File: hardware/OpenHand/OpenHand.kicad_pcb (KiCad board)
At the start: 4 copper layers, 110 x 50 mm, 214 parts, among them J1 CONN_MOTOR_1, J10 CONN_JTAG, J11 CONN_FDBK_2, J12 CONN_EMG_2, J13 CONN_POS_3, J2 CONN_MOTOR_2, J3 CONN_BATT, J4 CONN_POS_1, J5 USB_C_CONN, J6 CONN_MOTOR_3, J7 CONN_FDBK_1, J8 CONN_EMG_1, J9 CONN_POS_2, Q1 AO3401A, SW1 BTN_RST, SW2 BTN_BOOT, SW3 SW_Push, U1 STM32F103RETx, U10 DRV8833PWP, U2 TPS565201DDCR, U3 AMS1117-3.3, U4 LT1175-5_SOT223, U5 LM324, U6 LM324, U7 DRV8833PWP, U8 DRV8833PWP, U9 DRV8833PWP

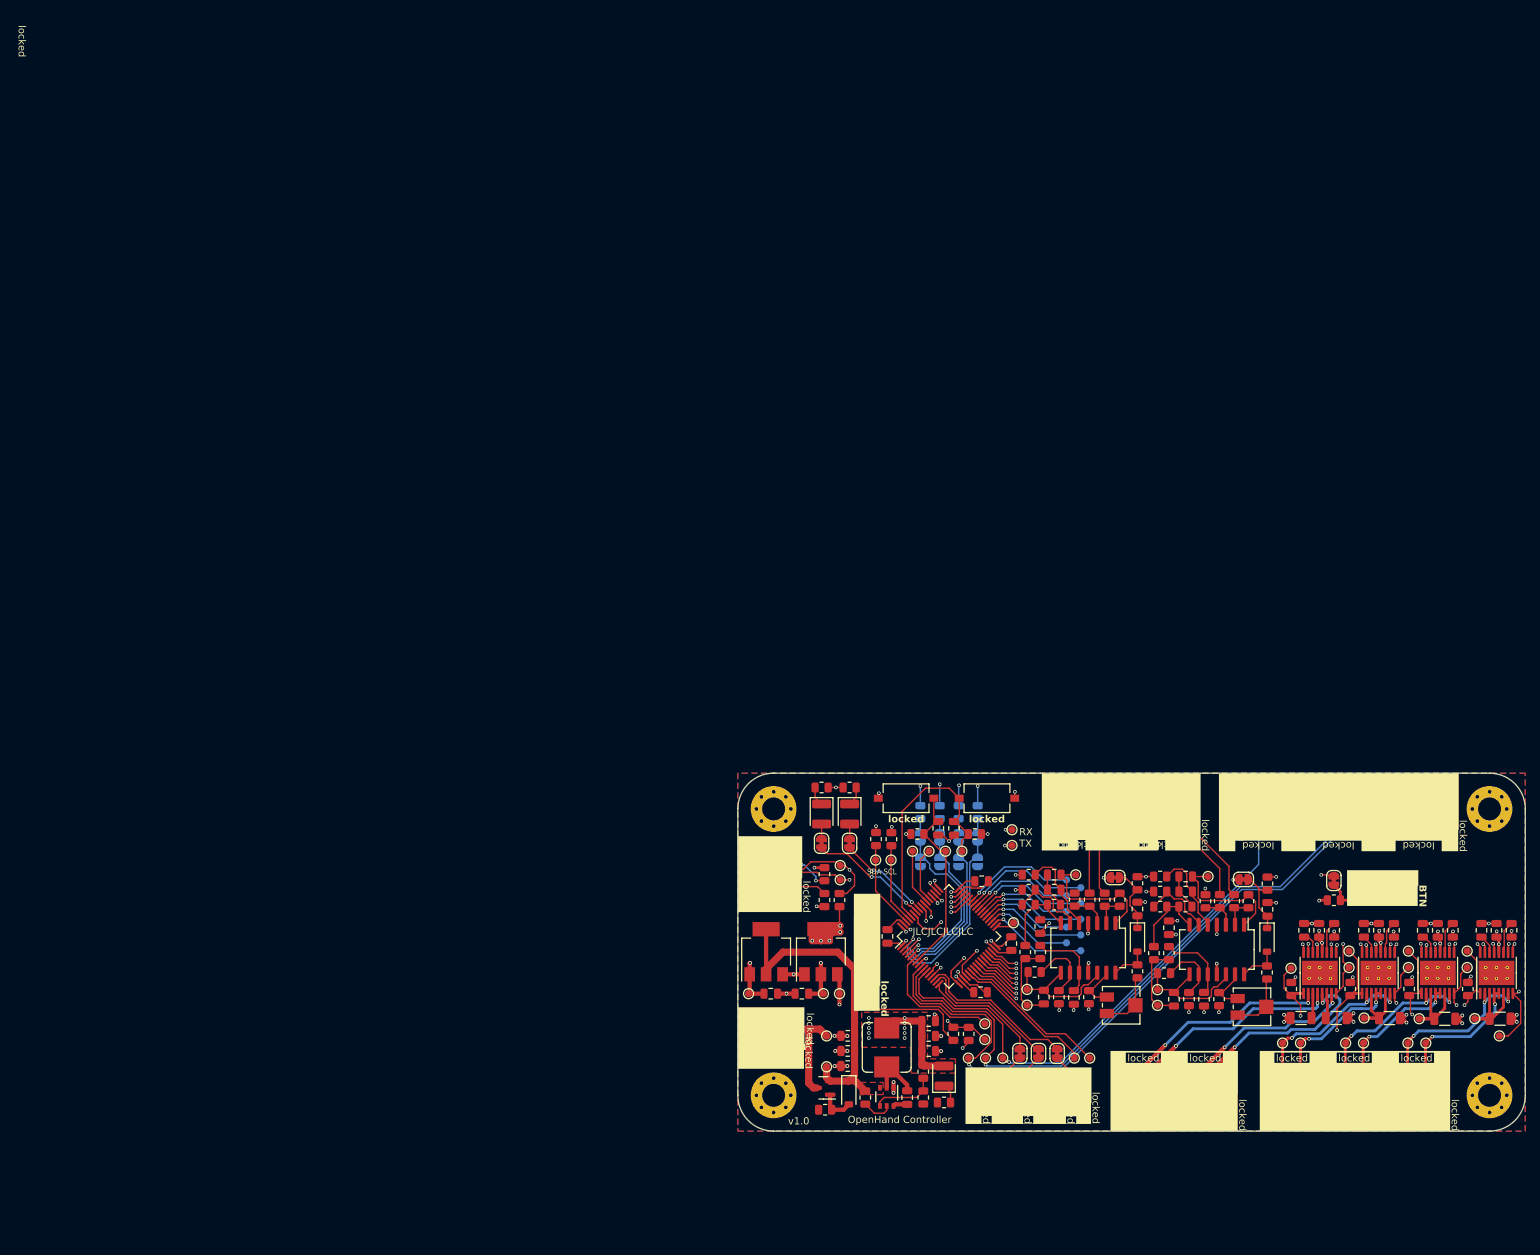
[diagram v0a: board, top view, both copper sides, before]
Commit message: Update PCB design/layout
Still WIP, routing traces currently
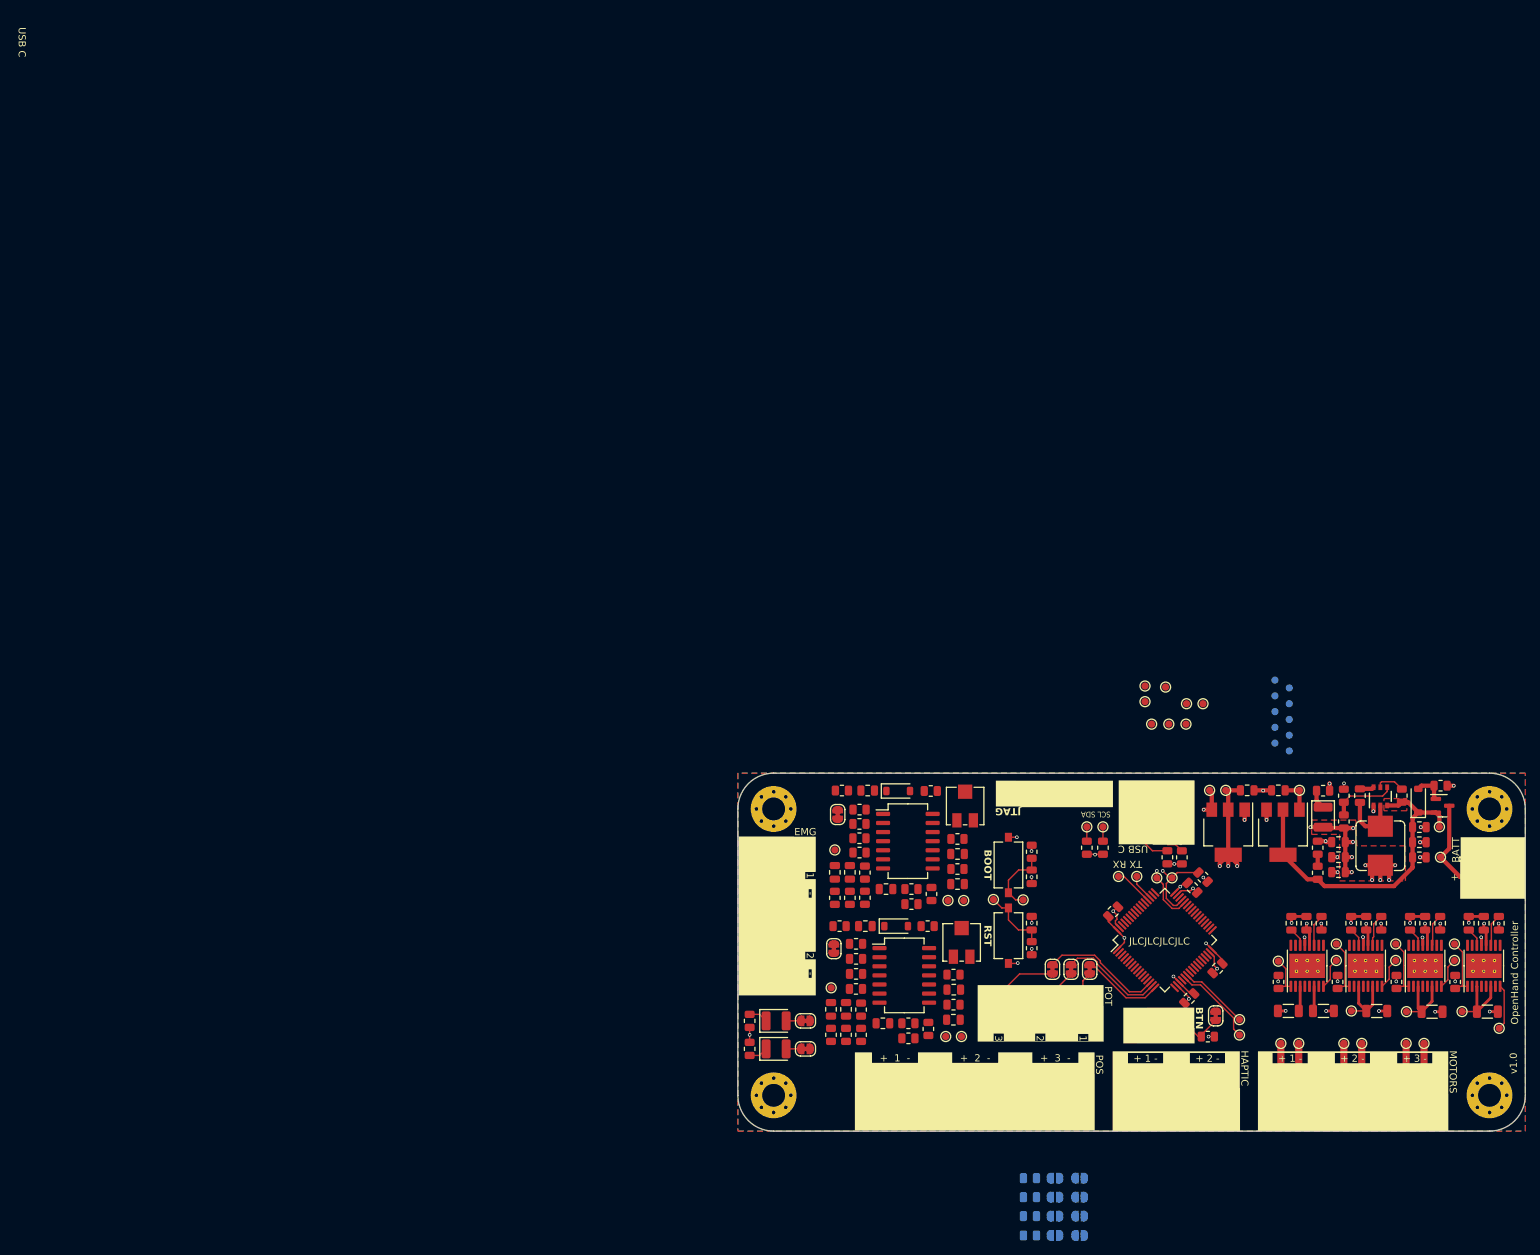
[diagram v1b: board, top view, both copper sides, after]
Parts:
- moved J3 99.3 mm to (203.0, 112.0), turned to -90 degrees
- moved R19 97.2 mm to (198.2, 101.8), turned to 180 degrees
- moved Q1 95.0 mm to (198.4, 104.5), turned to 0 degrees
- moved TP20 91.9 mm to (198.0, 107.5), turned to 180 degrees
- moved D3 89.4 mm to (195.1, 103.8), turned to 90 degrees
- moved TP19 89.3 mm to (198.2, 111.8), turned to 180 degrees
- moved C9 86.5 mm to (195.2, 107.5), turned to 0 degrees
- moved R17 86.0 mm to (192.8, 103.1), turned to -90 degrees
- moved C7 85.0 mm to (195.2, 109.6), turned to 0 degrees
- moved C8 83.7 mm to (195.2, 111.8), turned to 0 degrees
- moved TP23 82.0 mm to (178.4, 102.4), turned to 180 degrees
- moved U2 80.7 mm to (189.8, 103.2), turned to 90 degrees
- moved J4 76.9 mm to (124.4, 142.7), turned to 180 degrees
- moved C15 76.4 mm to (175.5, 102.4), turned to 180 degrees
- moved C10 76.0 mm to (186.9, 103.1), turned to 90 degrees
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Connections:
- net Net-(C18-Pad1) renamed /Sensors/amp_out_1
- J10 pad 3: JTAG_TDI -> JTAG_TDO
- J10 pad 4: JTAG_TDO -> JTAG_TDI
- U1 pad 14: TRIM_POT_01 -> TRIM_POT_03
- U1 pad 16: TRIM_POT_03 -> TRIM_POT_01
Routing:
- net MOTOR_03_DIR: track 120.6 -> 0.00 mm, vias 3 -> 0
- net MOTOR_03_PWM: track 112.1 -> 0.00 mm, vias 3 -> 0
- net MOTOR_02_DIR: track 111.6 -> 0.00 mm, vias 3 -> 0
- net HALL_SENS_01_S: track 102.2 -> 0.00 mm, vias 1 -> 0
- net MOTOR_02_PWM: track 102.1 -> 0.00 mm, vias 3 -> 0
- net HALL_SENS_02_S: track 86.8 -> 0.00 mm, vias 1 -> 0
- net MOTOR_01_DIR: track 84.6 -> 0.00 mm, vias 3 -> 0
- net MOTOR_01_PWM: track 82.9 -> 0.00 mm, vias 3 -> 0
- net MOTOR_03_FAULT: track 89.3 -> 6.39 mm, vias 2 -> 0
- net MOTOR_03_EN: track 87.5 -> 8.25 mm, vias 2 -> 0
- net -5V: track 80.5 -> 4.70 mm, vias 3 -> 0
- net HALL_SENS_03_S: track 74.8 -> 0.00 mm, vias 1 -> 0
- net MOTOR_02_EN: track 79.8 -> 8.23 mm, vias 2 -> 0
- net MOTOR_02_FAULT: track 75.5 -> 4.37 mm, vias 2 -> 0
- net BTN_01: track 68.1 -> 0.00 mm, vias 2 -> 0
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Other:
- board text added: "+"
- board text added: "+ 1 -"
- board text added: "+ 2 -"
- board text added: "+ 3 -"
- board text added: "-"
- board text added: "BATT"
- board text added: "BOOT"
- board text added: "EMG"
- board text added: "GND RST TDO TDI TCK TMS"
- board text added: "HAPTIC"
- board text added: "JTAG"
- board text added: "MOTORS"
- board text added: "POS"
- board text added: "POT"
- board text added: "RST"
- board text added: "SCL SDA"
- board text added: "TX RX"
- board text added: "USB C"
- board text added: "github.com/AleksaHeler/ProstheticHand"
- board text removed: "RX TX"
- board text removed: "SDA SCL"
- board text removed: "locked"

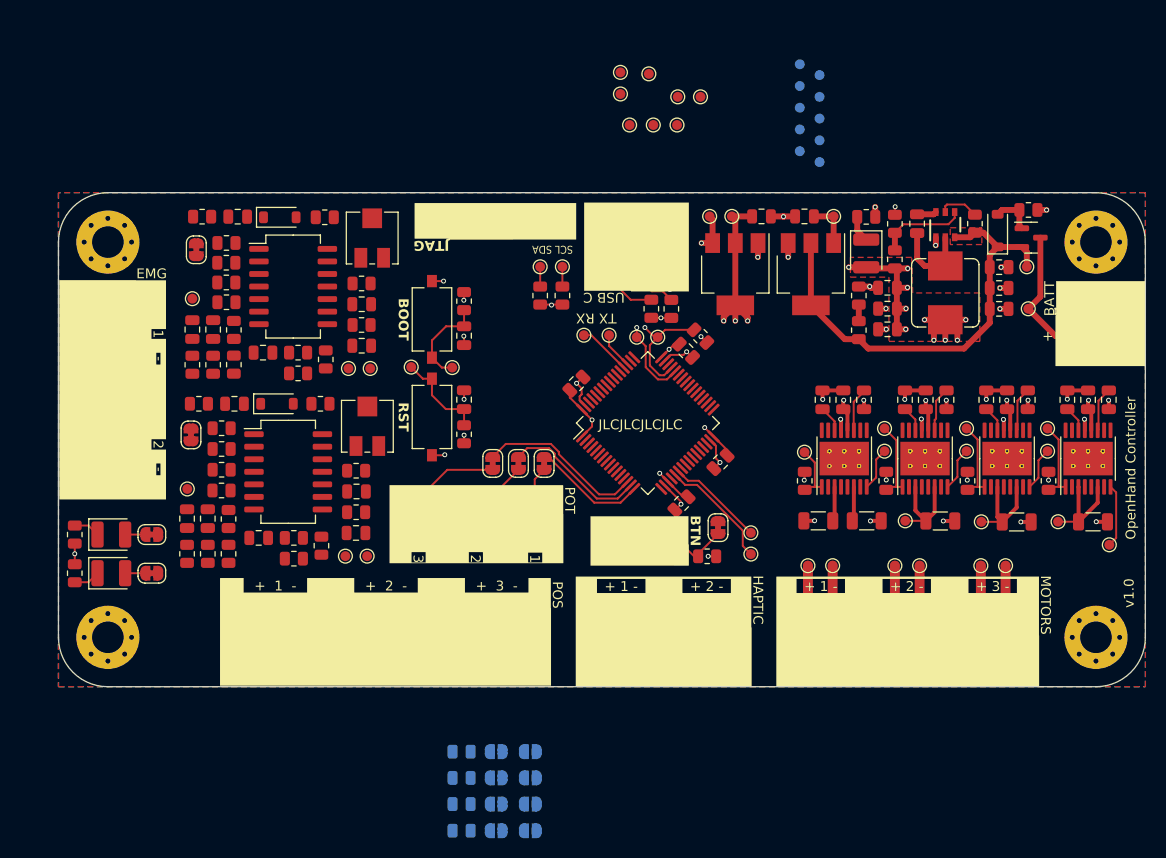
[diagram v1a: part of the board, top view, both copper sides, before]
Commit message: Update PCB, add STLs from hand model
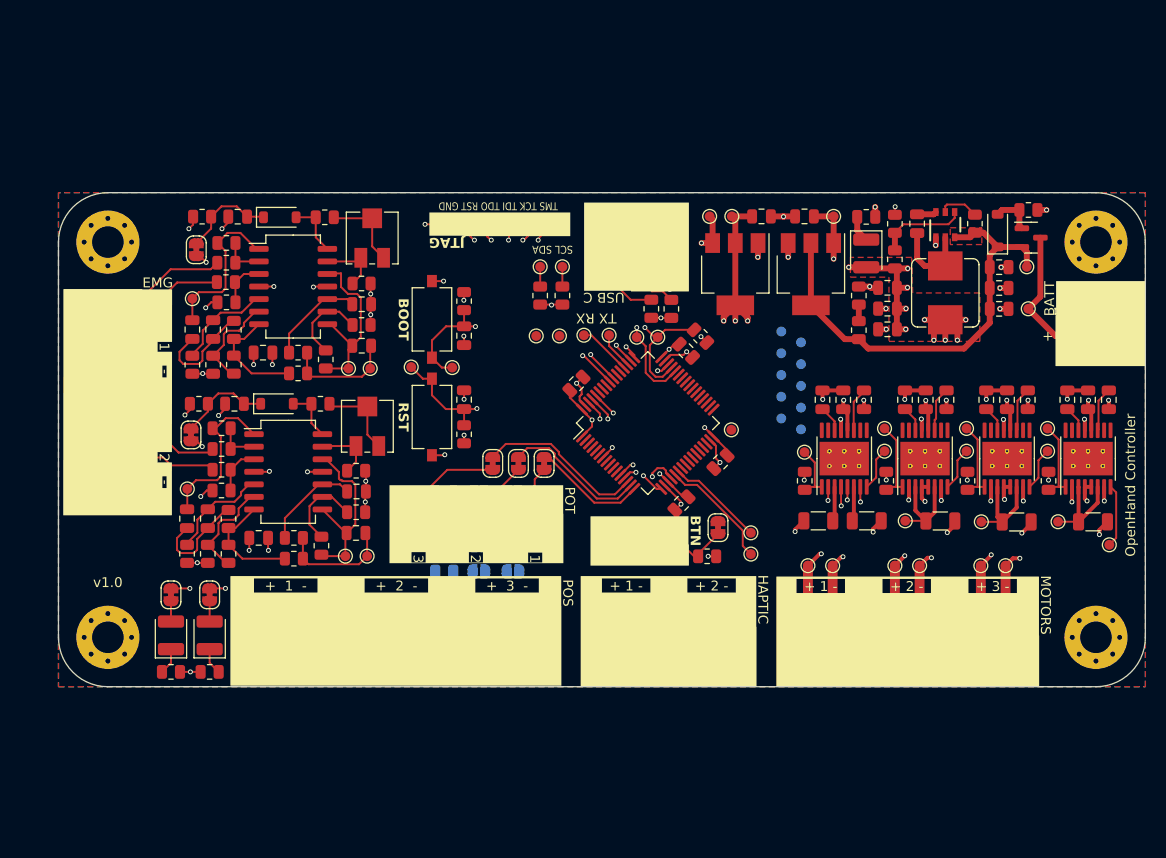
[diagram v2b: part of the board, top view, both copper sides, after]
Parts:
- removed the J10 at (137.9, 103.0)
- removed TP11: TP_HALL_02, TestPoint:TestPoint_Pad_D1.0mm
- removed the TP12 at (162.6, 93.2)
- removed TP15: TP_UC_PIN_PC12, TestPoint:TestPoint_Pad_D1.0mm
- removed the TP18 at (159.8, 88.0)
- added TP13: TP_UC_PIN_PD2, TestPoint:TestPoint_Pad_D1.0mm, F.Cu at (148.3, 114.5)
- added TP20: TP_UC_PIN_PC12, TestPoint:TestPoint_Pad_D1.0mm, F.Cu at (150.7, 114.5)
- added TP23: TP_UC_PIN_PB12, TestPoint:TestPoint_Pad_D1.0mm, F.Cu at (168.1, 124.0)
- added TP6: TP_JTAG_TCK, TestPoint:TestPoint_Pad_D1.0mm, F.Cu at (147.8, 103.2)
- added TP8: TP_JTAG_TDO, TestPoint:TestPoint_Pad_D1.0mm, F.Cu at (143.4, 103.2)
- TP10: value TP_HALL_01 -> TP_JTAG_GND
- TP5: value TP_UC_PIN_PD1 -> TP_JTAG_TMS
- TP7: value TP_UC_PIN_PD2 -> TP_JTAG_TDI
- TP9: value TP_BATT_SENSE -> TP_JTAG_RST
- moved TP41 27.1 mm to (175.2, 115.2)
- moved TP57 27.1 mm to (173.2, 120.7)
- moved TP42 27.1 mm to (175.2, 117.3)
- moved TP43 27.1 mm to (173.2, 114.0)
- moved TP44 27.1 mm to (173.2, 116.2)
- moved TP54 27.1 mm to (175.2, 119.5)
- moved TP55 27.1 mm to (175.2, 121.8)
- moved TP56 27.1 mm to (173.2, 118.5)
- moved TP60 27.1 mm to (175.2, 124.0)
- moved TP61 27.1 mm to (173.2, 122.8)
- moved JP10 26.3 mm to (142.6, 138.3)
- moved JP11 26.3 mm to (146.0, 130.3)
- moved JP12 26.3 mm to (146.0, 133.0)
- moved JP13 26.3 mm to (146.0, 135.7)
- moved JP14 26.3 mm to (146.0, 138.3)
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- renumbered J11 to J10, J12 to J11, J13 to J12, TP6 to TP12, TP8 to TP14, TP13 to TP18, TP14 to TP19, TP16 to TP21, TP17 to TP22, TP19 to TP24, TP20 to TP25, TP21 to TP26, TP22 to TP27, TP23 to TP28, TP24 to TP29, TP25 to TP30, TP26 to TP31, TP27 to TP32, TP28 to TP33, TP29 to TP34, TP30 to TP35, TP31 to TP36, TP32 to TP37, TP33 to TP38, TP34 to TP39, TP35 to TP40, TP36 to TP41, TP37 to TP42, TP38 to TP43, TP39 to TP44, TP40 to TP45, TP41 to TP46, TP42 to TP47, TP43 to TP48, TP44 to TP49, TP45 to TP50, TP46 to TP51, TP47 to TP52, TP48 to TP53, TP49 to TP54, TP50 to TP55, TP51 to TP56, TP52 to TP57, TP53 to TP58, TP54 to TP59, TP55 to TP60, TP56 to TP61
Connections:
- R11 pad 1: Net-(U1-PC0) -> /BATT_SENSE
- R12 pad 2: Net-(U1-PC0) -> /BATT_SENSE
- TP10 pad 1: HALL_SENS_01_S -> Earth
- TP5 pad 1: Net-(U1-PD1) -> JTAG_TMS
- TP7 pad 1: Net-(U1-PD2) -> JTAG_TDI
- TP9 pad 1: Net-(U1-PC0) -> JTAG_RST
- U1 pad 6: Net-(U1-PD1) -> unconnected-(U1-PD1-Pad6)
- U1 pad 8: Net-(U1-PC0) -> /BATT_SENSE
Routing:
- net -5V: track 4.70 -> 65.2 mm, vias 0 -> 3
- net EMG_01_UC: track 0.00 -> 57.1 mm, vias 0 -> 2
- net EMG_02_UC: track 0.00 -> 52.4 mm, vias 0 -> 2
- net Earth: track 67.5 -> 96.9 mm, vias 42 -> 58
- net HAPTIC_01_P: track 0.00 -> 28.6 mm, vias 0 -> 1
- net HAPTIC_01_N: track 0.00 -> 27.1 mm, vias 0 -> 1
- net HAPTIC_02_P: track 0.00 -> 23.7 mm, vias 0 -> 1
- net JTAG_RST: track 0.00 -> 22.1 mm, vias 0 -> 2
- net JTAG_TMS: track 0.00 -> 22.0 mm, vias 0 -> 2
- net UC_BOOT: track 9.69 -> 30.9 mm, vias 0 -> 2
- net MOTOR_03_P: track 5.09 -> 26.1 mm, vias 0 -> 3
- net JTAG_TDO: track 0.00 -> 20.9 mm, vias 0 -> 2
- net MOTOR_01_P: track 5.10 -> 25.7 mm, vias 0 -> 3
- net MOTOR_02_P: track 5.12 -> 25.6 mm, vias 0 -> 3
- net JTAG_TDI: track 0.00 -> 19.8 mm, vias 0 -> 2
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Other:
- board text added: "TMS TCK TDI TDO RST GND"
- board text removed: "GND RST TDO TDI TCK TMS"
